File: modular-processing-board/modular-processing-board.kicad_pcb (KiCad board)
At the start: 6 copper layers, 90 x 90 mm, 165 parts, among them J1001 BWU.FL-IPEX1, J202 Conn_02x06_Odd_Even, J401 TF01A, J501 Plug_Hirose_DF40_2x40_DF40C-8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, J502 Conn_02x06_Odd_Even, J601 Conn_Coaxial_Small, J602 BWU.FL-IPEX1, J604 Conn_Coaxial_Small, J701 Conn_02x02_Odd_Even, J801 TYPE-C-31-M-12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

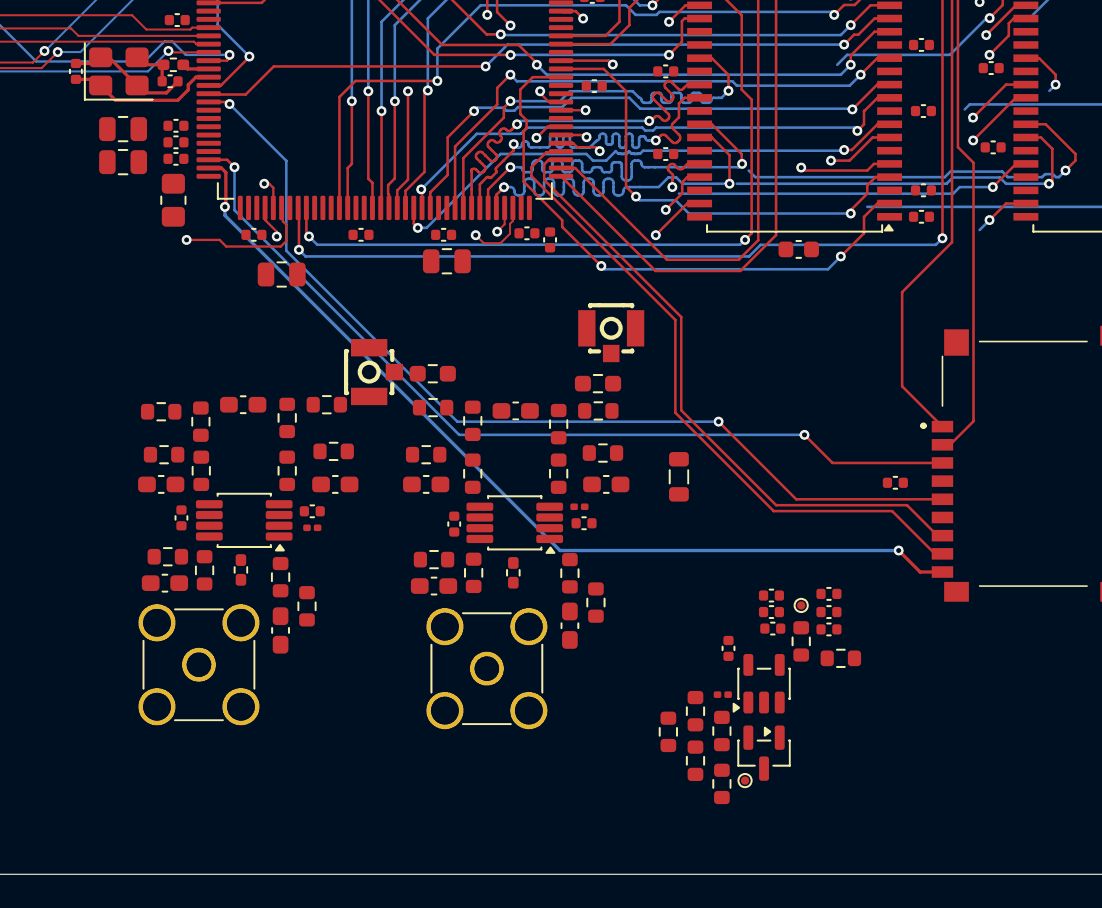
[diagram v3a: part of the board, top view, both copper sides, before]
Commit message: redid frontend layout, routed diff adc wires (next) finish routing, start with decoupling and planes
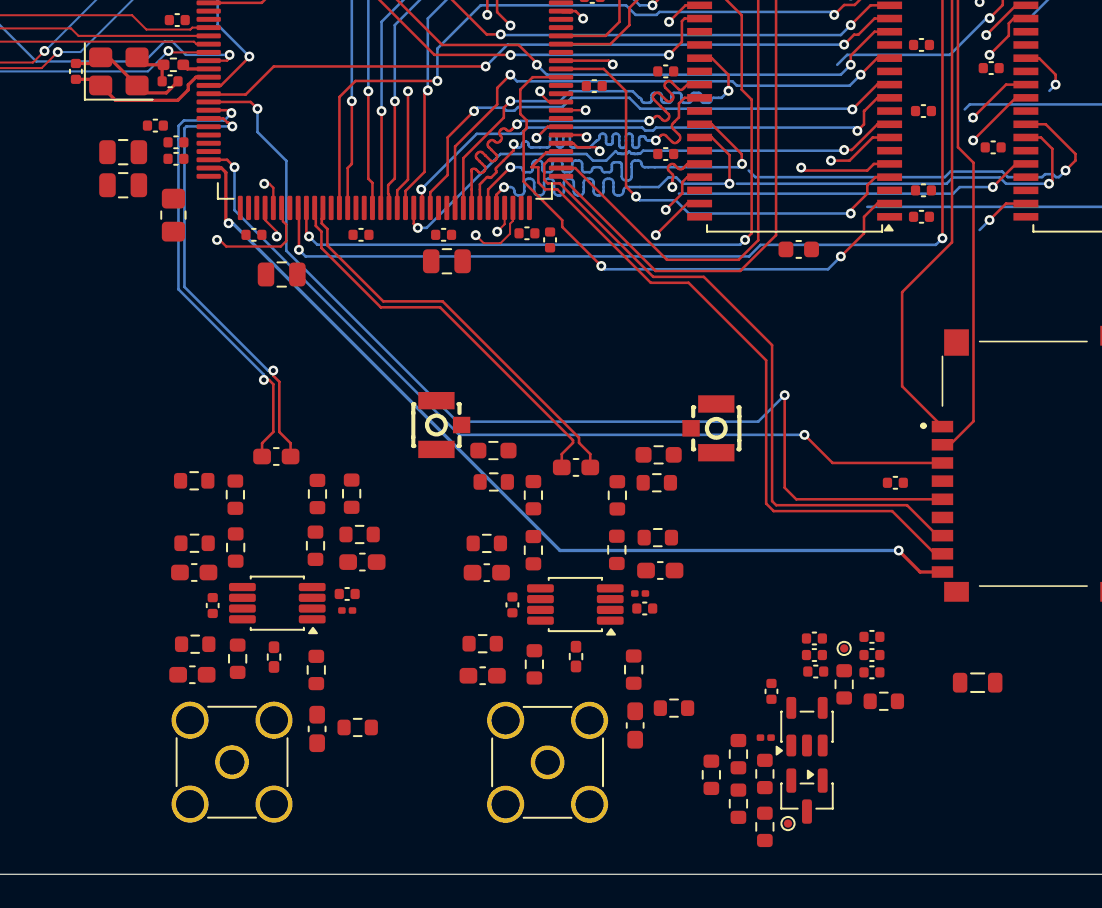
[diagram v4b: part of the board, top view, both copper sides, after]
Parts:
- moved L701 22.0 mm to (117.9, 126.4), turned to 180 degrees
- moved R608 7.95 mm to (80.4, 129.1), turned to 0 degrees
- moved R1006 7.95 mm to (99.5, 127.9), turned to 180 degrees
- moved J1001 7.70 mm to (101.3, 111.0), turned to 0 degrees
- moved C612 7.22 mm to (97.2, 129.0)
- moved R1013 7.00 mm to (97.1, 125.6)
- moved J601 6.76 mm to (91.8, 131.2)
- moved R1021 6.65 mm to (91.0, 125.3)
- moved R1024 6.50 mm to (88.2, 118.0)
- moved C1016 6.48 mm to (88.2, 119.7)
- moved C1025 6.41 mm to (97.5, 121.0)
- moved C610 6.36 mm to (77.9, 129.2)
- moved C1024 6.33 mm to (97.7, 121.9)
- moved R1015 6.33 mm to (93.6, 124.8)
- moved J604 6.23 mm to (72.8, 131.2)
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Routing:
- net /adc-frontend/MCU_ADC3_DIRECT_INN0: track 0.00 -> 27.8 mm, vias 0 -> 2
- net /adc-frontend/MCU_ADC3_DIRECT_INP0: track 0.00 -> 27.3 mm, vias 0 -> 2
- net /adc-frontend/MCU_ADC12_FAST_INN5: track 0.00 -> 24.6 mm
- net /adc-frontend/MCU_ADC12_FAST_INP5: track 0.00 -> 24.6 mm
- net /mcu/SDMMC.CK: track 57.6 -> 63.0 mm
- net /mcu/SDMMC.D0: track 38.4 -> 40.7 mm
- net /mcu/SDMMC.D1: track 40.5 -> 42.5 mm
- net /connectors/PSSI.D13: track 46.3 -> 47.3 mm
- net /connectors/PSSI.D12: track 49.9 -> 50.9 mm

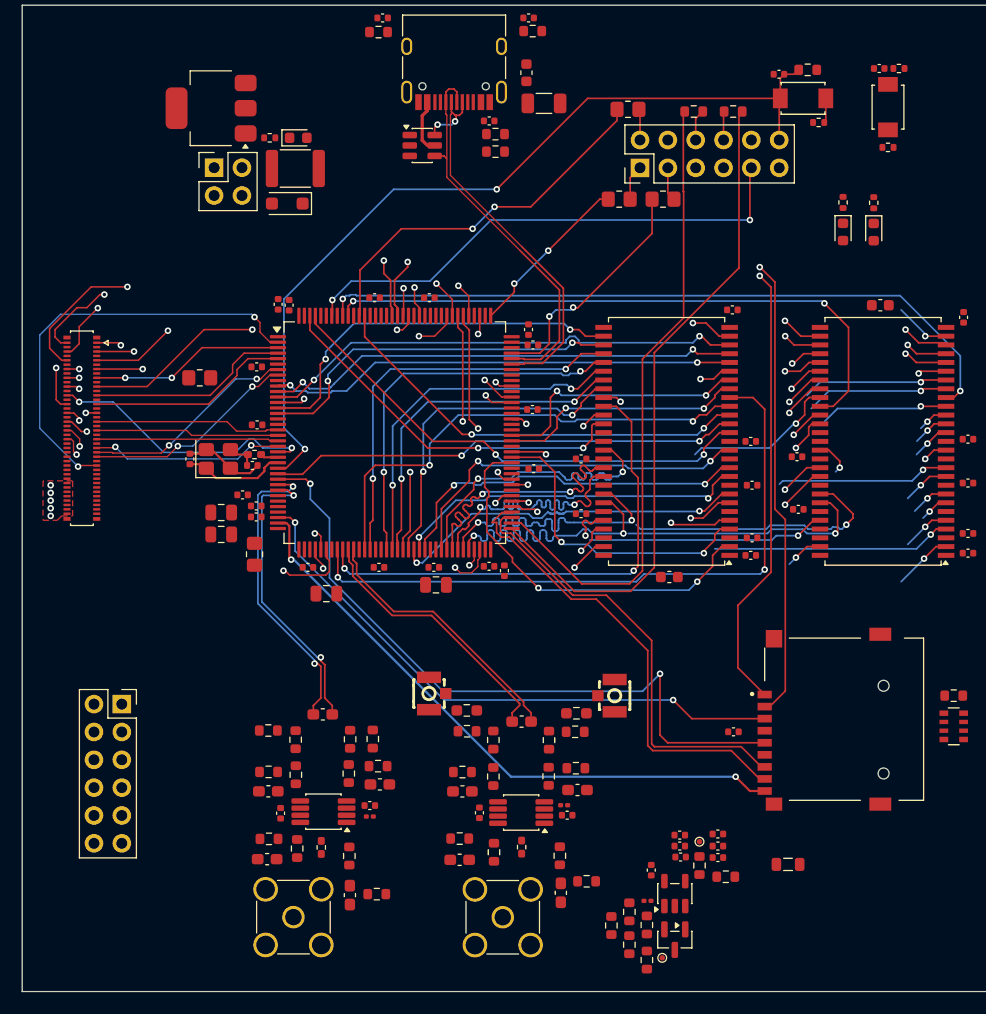
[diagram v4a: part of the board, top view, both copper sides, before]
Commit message: reconnected vref
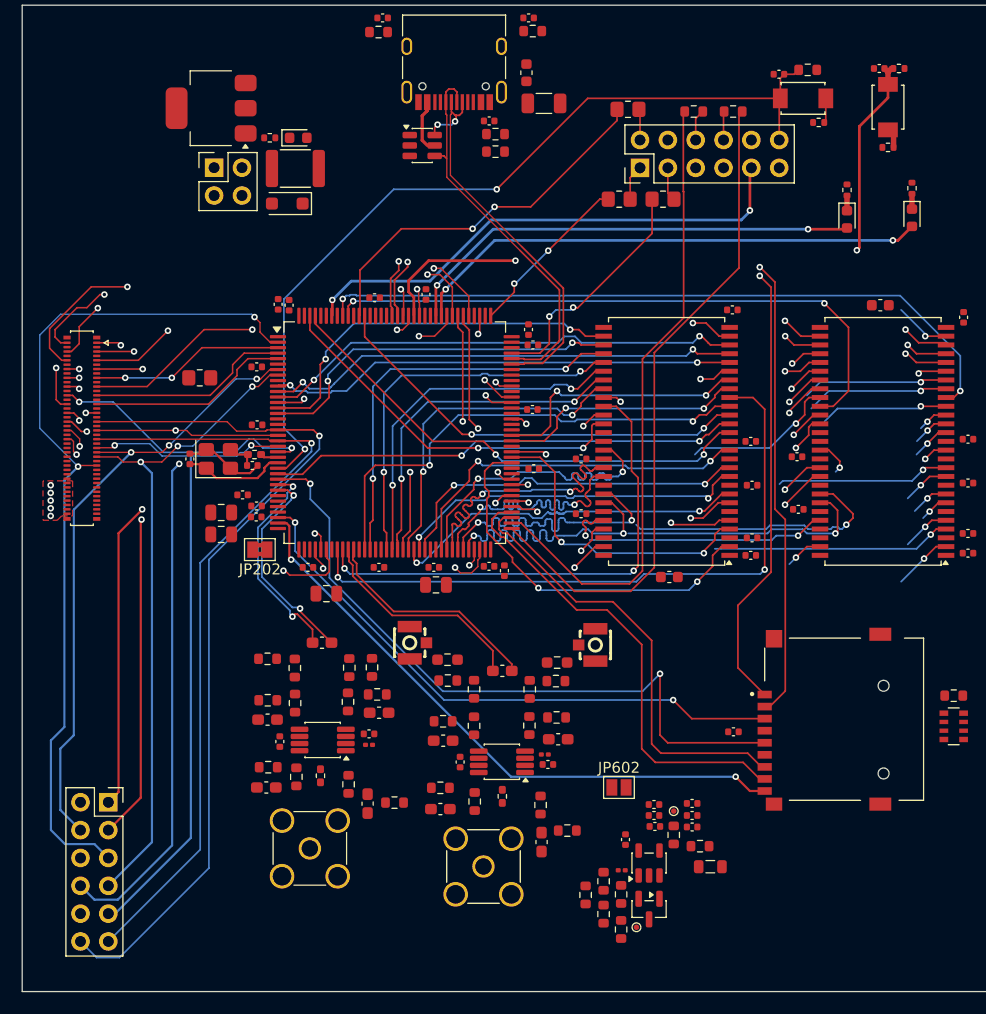
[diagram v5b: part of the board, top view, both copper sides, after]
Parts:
- removed R211: 0, Resistor_SMD:R_0805_2012Metric_Pad1.20x1.40mm_HandSolder
- added JP202: SolderJumper_2_Bridged, Jumper:SolderJumper-2_P1.3mm_Bridged2Bar_Pad1.0x1.5mm, F.Cu at (69.7, 97.7)
- added JP602: SolderJumper_2_Open, Jumper:SolderJumper-2_P1.3mm_Open_Pad1.0x1.5mm, F.Cu at (102.5, 119.4)
- moved J502 9.04 mm to (55.9, 120.7)
- moved R608 8.51 mm to (82.0, 120.8)
- moved C610 8.51 mm to (79.5, 120.8)
- moved L701 7.09 mm to (110.8, 126.6)
- moved C616 6.54 mm to (71.5, 115.2)
- moved C617 6.54 mm to (79.6, 114.5)
- moved C618 6.54 mm to (79.6, 115.5)
- moved R611 6.54 mm to (80.4, 110.9)
- moved R614 6.54 mm to (77.8, 108.4)
- moved R619 6.54 mm to (73.0, 118.4)
- moved C614 6.54 mm to (70.3, 119.4)
- moved C615 6.54 mm to (70.4, 113.2)
- moved R610 6.54 mm to (70.4, 107.6)
- moved R615 6.54 mm to (77.7, 111.6)
- moved U603 6.54 mm to (75.4, 115.0)
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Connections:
- net /connectors/ADC_ALERT renamed /connectors/AD_ALERT
- C218 pad 1: VDDA -> /adc-frontend/MCU_VREF
- C219 pad 1: VDDA -> /adc-frontend/MCU_VREF
- U201 pad 32: Net-(U201-VREF+) -> /adc-frontend/MCU_VREF
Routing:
- net /mcu/BUTTON_1: track 0.00 -> 63.9 mm, vias 0 -> 2
- net /connectors/PWM.0_HI: track 16.9 -> 80.3 mm, vias 0 -> 1
- net /connectors/PWM.0_LI: track 16.6 -> 72.8 mm, vias 0 -> 1
- net /connectors/PWM.1_HI: track 16.7 -> 66.3 mm, vias 0 -> 2
- net /mcu/LED_2: track 0.00 -> 47.5 mm, vias 0 -> 2
- net /connectors/PWM.1_LI: track 17.6 -> 63.0 mm
- net /mcu/LED_1: track 0.00 -> 42.4 mm, vias 0 -> 2
- net /connectors/PSEPIC_EN: track 19.6 -> 60.8 mm, vias 2 -> 3
- net /connectors/AD_ALERT: track 39.3 -> 79.8 mm
- net /connectors/PBOOST_EN: track 19.7 -> 57.6 mm, vias 2 -> 3
- net /connectors/I2C.SCL: track 45.6 -> 75.4 mm, vias 2 -> 3
- net /connectors/I2C.SDA: track 46.7 -> 74.7 mm, vias 2 -> 3
- net /adc-frontend/MCU_ADC3_DIRECT_INN0: track 27.8 -> 19.8 mm
- net /adc-frontend/MCU_ADC3_DIRECT_INP0: track 27.3 -> 19.3 mm
- net /adc-frontend/MCU_ADC12_FAST_INN5: track 24.6 -> 20.0 mm
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
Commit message: routing hardware (next) reroute the CLK and A12
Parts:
- J401: value TF01A -> TF-01A
- moved R203 7.69 mm to (67.8, 75.2)
- moved C616 4.51 mm to (75.3, 112.8), turned to 180 degrees
- moved C619 4.38 mm to (91.5, 114.5), turned to 180 degrees
- moved C207 1.76 mm to (69.8, 92.2), turned to 90 degrees
- moved C306 0.89 mm to (133.9, 88.4), turned to -90 degrees
- moved C305 0.63 mm to (133.8, 98.4), turned to -90 degrees
- moved R613 0.55 mm to (77.4, 118.7)
- moved C310 0.54 mm to (133.9, 91.3), turned to 90 degrees
- moved C309 0.50 mm to (133.8, 96.1), turned to 90 degrees
- moved C311 0.36 mm to (133.8, 76.8)
- moved C307 0.26 mm to (118.8, 94.3)
- moved R201 0.12 mm to (128.1, 53.8)
- moved C308 0.12 mm to (118.8, 89.3)
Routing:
- net GND: track 7.51 -> 136.0 mm, vias 0 -> 75
- net +3V3: track 0.00 -> 41.6 mm
- net /mcu/USB_SENSE: track 0.00 -> 28.8 mm, vias 0 -> 2
- net /mcu/SDRAM.A0: track 46.5 -> 67.8 mm
- net /mcu/SDRAM.A6: track 40.3 -> 61.3 mm
- net /power/USB_VBUS: track 5.00 -> 25.7 mm
- net /mcu/SDRAM.A4: track 39.1 -> 59.6 mm
- net /mcu/SDRAM.A11: track 34.3 -> 54.7 mm
- net /mcu/SDRAM.~{CAS}: track 42.5 -> 62.7 mm
- net /mcu/SDRAM.A9: track 35.2 -> 55.3 mm
- net /mcu/SDRAM.A10: track 43.4 -> 63.6 mm
- net /mcu/SDRAM.A8: track 36.0 -> 55.8 mm
- net /mcu/SDRAM.A1: track 47.3 -> 66.6 mm
- net /mcu/SDRAM.A3: track 49.8 -> 69.0 mm
- net /mcu/SDRAM.A7: track 39.0 -> 57.7 mm
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- added copper zone on In1.Cu, net GND
- added copper zone on In4.Cu, net GND

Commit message: added GND conconnections (next) remove 8th layer
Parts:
- moved C804 3.48 mm to (80.8, 52.6)
- moved R804 3.48 mm to (80.4, 53.9)
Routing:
- net GND: track 136.0 -> 174.3 mm, vias 75 -> 111
- net /power/USB_VBUS: track 25.7 -> 50.8 mm, vias 0 -> 6
- net /mcu/SDRAM.D2: track 42.0 -> 65.7 mm
- net /mcu/SDRAM.D3: track 41.3 -> 63.6 mm
- net /mcu/SDRAM.~{WE}: track 46.5 -> 68.7 mm
- net /mcu/SDRAM.D15: track 35.6 -> 55.7 mm
- net /mcu/SDRAM.D4: track 36.8 -> 56.7 mm
- net /mcu/SDRAM.UDQM: track 37.8 -> 57.7 mm
- net /mcu/SDRAM.D8: track 31.0 -> 50.7 mm
- net /mcu/SDRAM.D7: track 36.7 -> 56.3 mm
- net /mcu/SDRAM.D9: track 30.8 -> 50.3 mm
- net /mcu/SDRAM.LDQM: track 49.0 -> 68.4 mm
- net /mcu/SDRAM.D10: track 30.9 -> 50.1 mm
- net /mcu/SDRAM.D0: track 40.8 -> 59.4 mm
- net /mcu/SDRAM.D5: track 36.9 -> 54.9 mm
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- added copper zone on F.Cu, net /power/LDO_OUT
- added copper zone on F.Cu, net GND
- added copper zone on F.Cu, net Net-(J701-Pin_2)
